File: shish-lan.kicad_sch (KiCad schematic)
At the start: 0 parts

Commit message: CuPhy: adding ports
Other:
- removed sheet buck_1V1
- removed sheet buck_2V5
- removed sheet buck_3V3
- removed sheet switch_decoupling
- removed sheet switch_gpios
- removed sheet switch_power
- added sheet switch_lan96455F (switch.kicad_sch)

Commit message: updating the projects
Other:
- sheet switch_lan96455F ports: added 1V1_EN, 25M_CLK_SWITCH, 2V5_EN, 3V3_EN, GGND, MIIM{MDIO,MDC}, PTP[0..3], RGMII{TXD[0..3], TX_CLK, TX_CTLR, RXD[0..3], RX_CLK, RX_CTLR}, SPI_SLV{DI,DO,nCS,CLK}, nRST_SWITCH; removed RGMII{TXD[0..3], TX_CLK, TX_CTLR, RXD[0..3], RX_CLK, RX_CTLR, MDIO, MDC},REF_CLK
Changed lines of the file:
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@@
 	)
 	(sheet
-		(at 191.77 45.72)
-		(size 91.44 41.91)
+		(at 182.88 44.45)
+		(size 91.44 92.71)
 		(exclude_from_sim no)
 		(in_bom yes)
@@
 		)
 		(property "Sheetname" "switch_lan96455F"
-			(at 191.77 45.0084 0)
+			(at 182.88 43.7384 0)
 			(effects
 				(font
@@
 		)
 		(property "Sheetfile" "switch.kicad_sch"
-			(at 191.77 88.2146 0)
+			(at 182.88 137.7446 0)
 			(effects
 				(font
@@
 		)
 		(pin "5-12V_INPUT" input
-			(at 191.77 50.8 180)
+			(at 182.88 113.03 180)
 			(effects
 				(font
@@
 			)
 		)
-		(pin "RGMII{TXD[0..3], TX_CLK, TX_CTLR, RXD[0..3], RX_CLK, RX_CTLR, MDIO, MDC},REF_CLK"
-			bidirectional
-			(at 191.77 55.88 180
-			)
+		(pin "RGMII{TXD[0..3], TX_CLK, TX_CTLR, RXD[0..3], RX_CLK, RX_CTLR}" bidirectional
+			(at 182.88 63.5 180)
 			(effects
 				(font
+					(size 1.27 1.27)
+				)
+				(justify left)
+			)
+		)
+		(pin "MIIM{MDIO,MDC}" bidirectional
+			(at 182.88 68.58 180)
+			(effects
+				(font
+					(size 1.27 1.27)
+				)
+				(justify left)
+			)
+		)
+		(pin "GGND" input
+			(at 182.88 115.57 180)
+			(effects
+				(font
+					(size 1.27 1.27)
+				)
+				(justify left)
+			)
+		)
+		(pin "nRST_SWITCH" input
+			(at 182.88 92.71 180)
+			(effects
+				(font
+					(size 1.27 1.27)
+				)
+				(justify left)
+			)
+		)
+		(pin "PTP[0..3]" input
+			(at 182.88 85.09 180)
+			(effects
+				(font
+					(size 1.27 1.27)
+				)
+				(justify left)
+			)
+		)
+		(pin "SPI_SLV{DI,DO,nCS,CLK}" bidirectional
+			(at 182.88 73.66 180)
+			(effects
+				(font
+					(size 1.27 1.27)
+				)
+				(justify left)
+			)
+		)
+		(pin "25M_CLK_SWITCH" input
+			(at 182.88 55.88 180)
+			(effects
+				(font
+					(size 1.27 1.27)
+				)
+				(justify left)
+			)
+		)
+		(pin "2V5_EN" input
+			(at 182.88 101.6 180)
+			(effects
+				(font
+					(size 1.27 1.27)
+				)
+				(justify left)
+			)
+		)
+		(pin "1V1_EN" input
+			(at 182.88 105.41 180)
+			(effects
+				(font
+					(size 1.27 1.27)
+				)
+				(justify left)
+			)
+		)
+		(pin "3V3_EN" input
+			(at 182.88 97.79 180)
+			(effects
+				(font

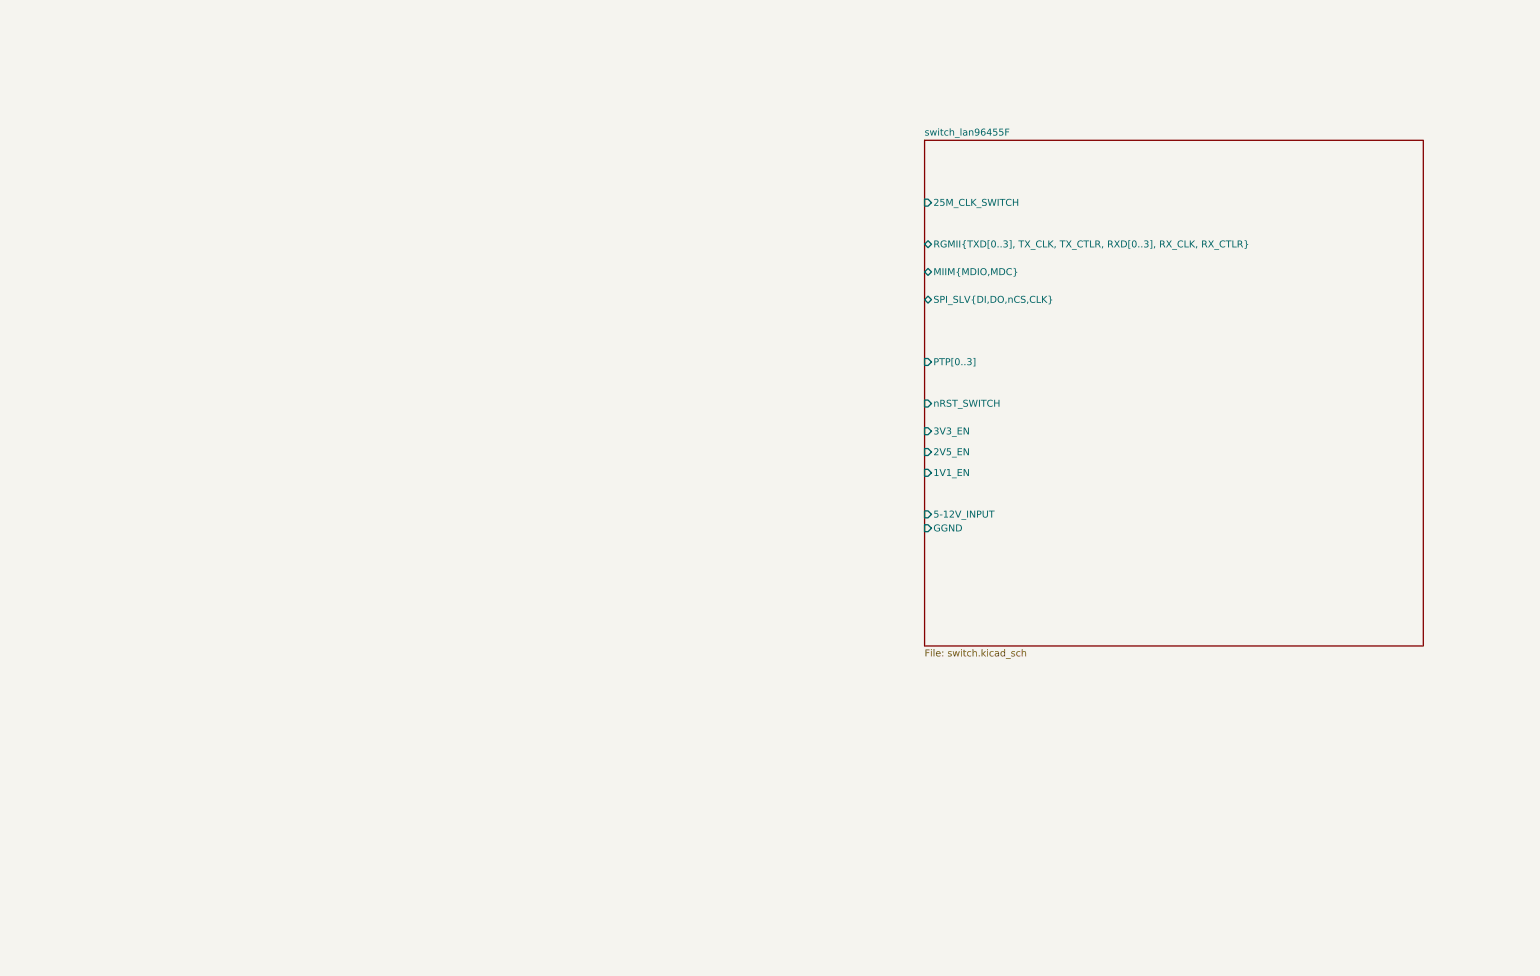
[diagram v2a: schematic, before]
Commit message: switch: finished 1st version
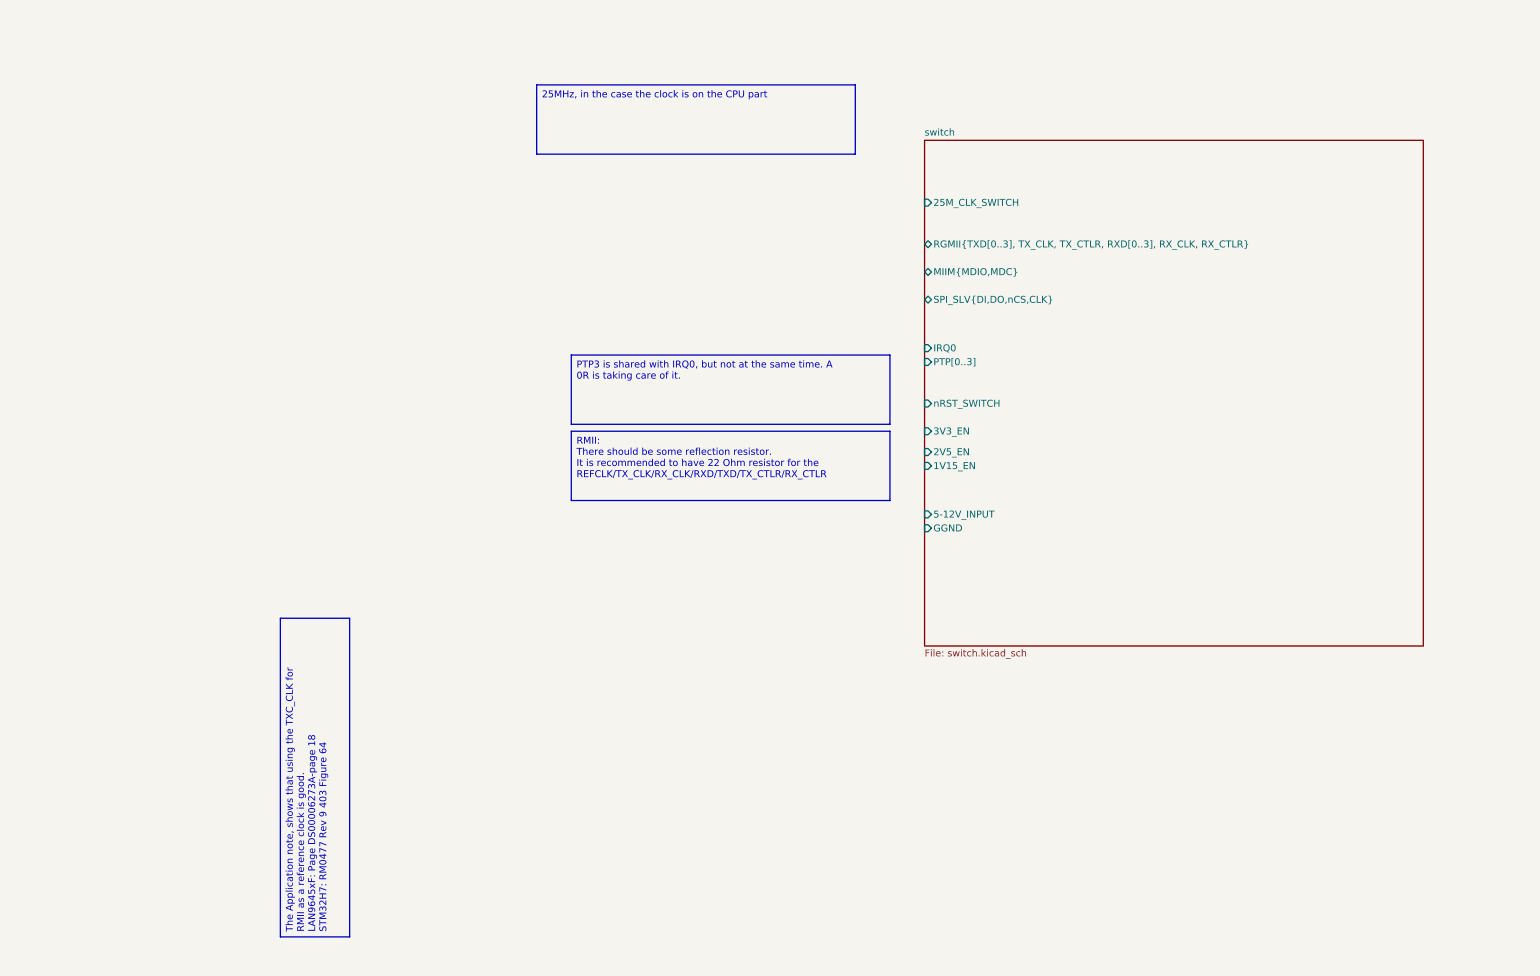
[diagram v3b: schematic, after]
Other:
- sheet switch_lan96455F renamed switch
- sheet switch ports: added 1V15_EN, IRQ0; removed 1V1_EN

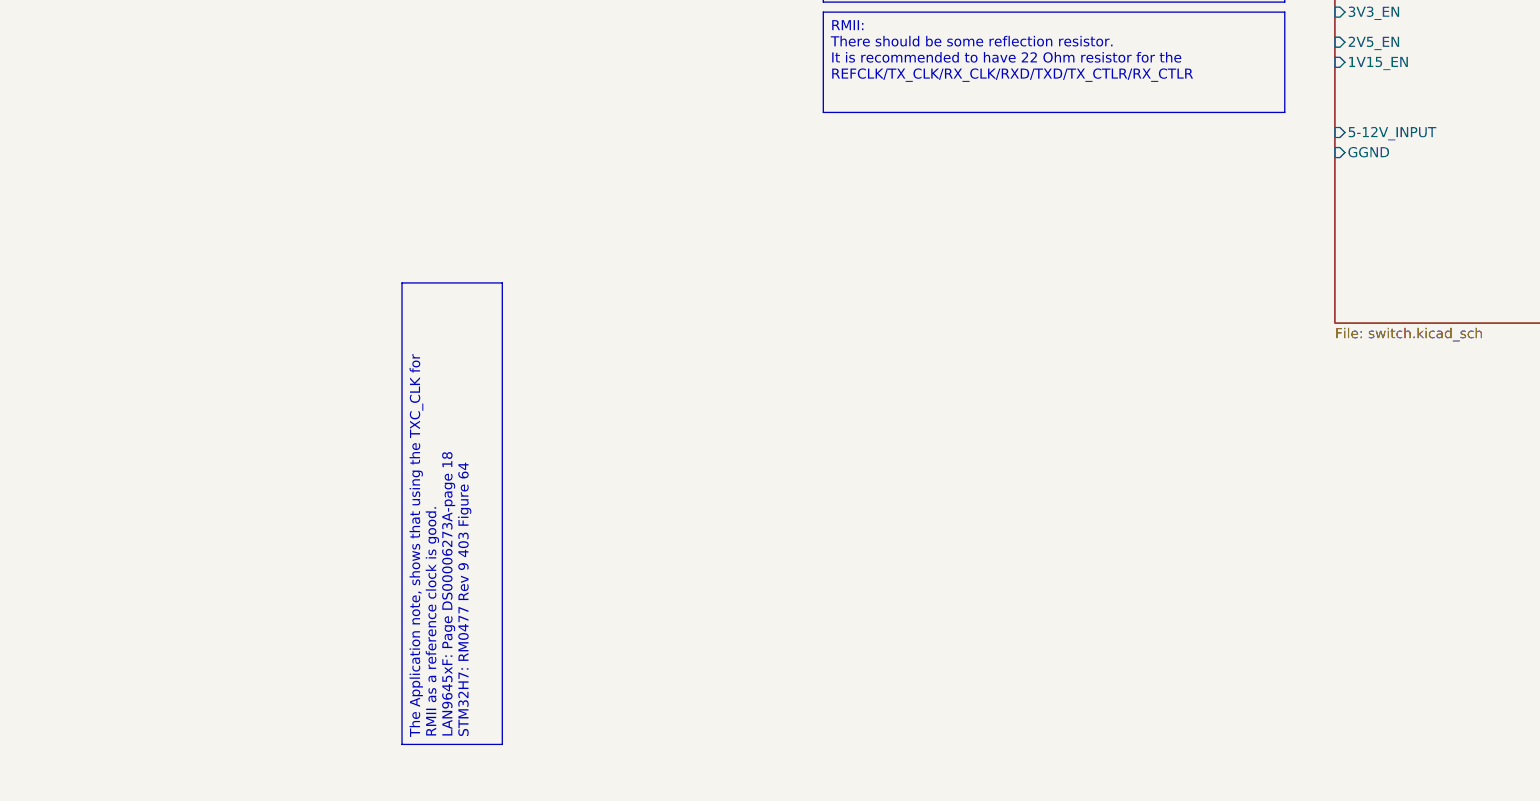
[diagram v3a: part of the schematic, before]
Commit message: adds GND test points because there is always one missing for the perfect measurement
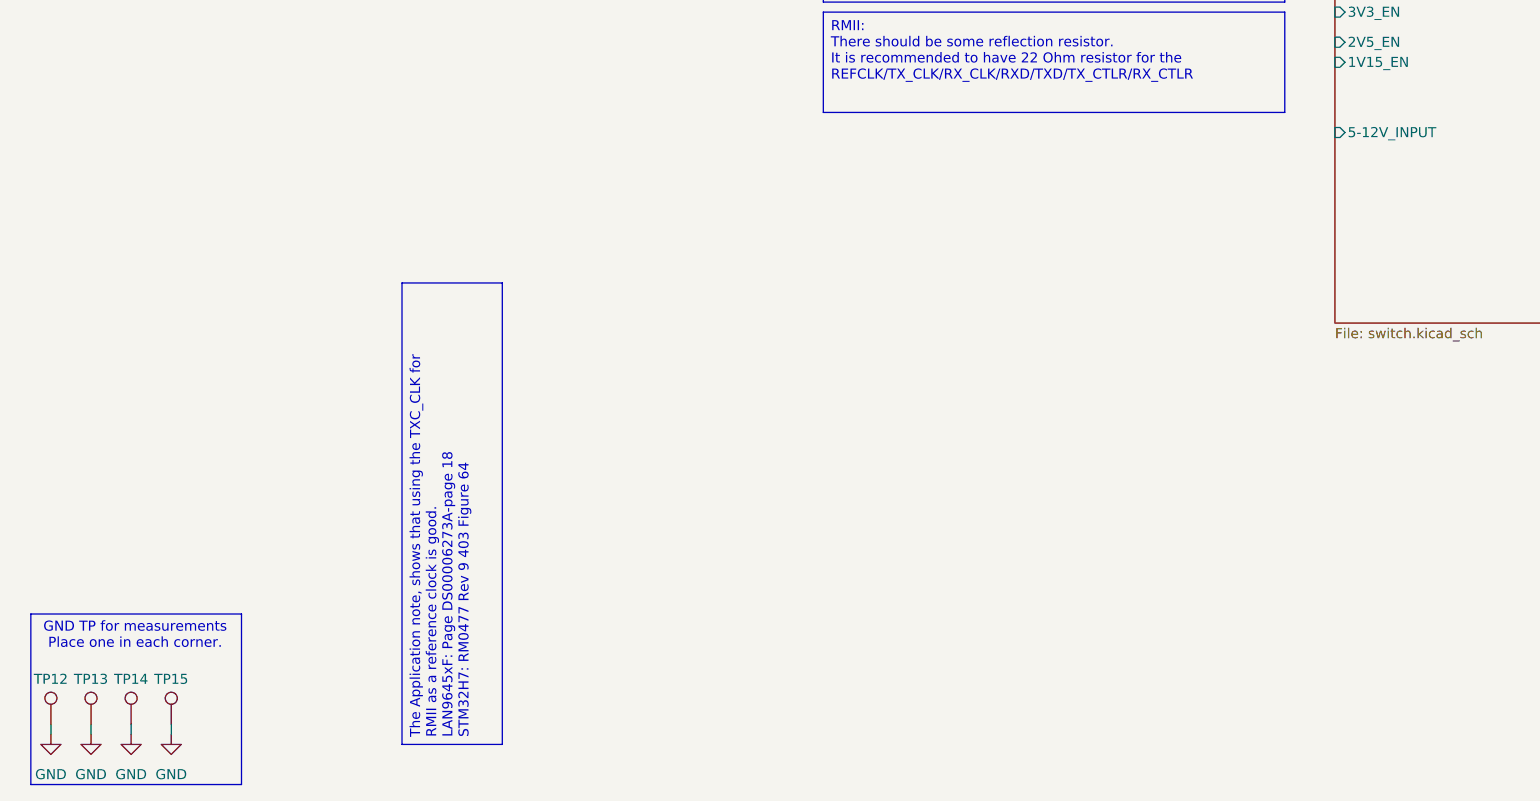
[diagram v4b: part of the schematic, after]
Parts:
- added TP12, TP13, TP14, TP15: ~, Connector_PinHeader_2.54mm:PinHeader_1x01_P2.54mm_Vertical, symbol KL_TP:TestPoint
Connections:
- new net GND: TP12.1, TP13.1, TP14.1, TP15.1
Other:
- sheet switch ports: added none; removed GGND
- note added: "GND TP for measurements Place one in each corner."

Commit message: updates project file and schematic. Refs: #1
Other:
- added sheet controller (controller.kicad_sch)
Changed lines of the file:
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@@
 	)
 	(sheet
-		(at 182.88 44.45)
-		(size 91.44 92.71)
+		(at 29.845 23.495)
+		(size 51.435 27.94)
 		(exclude_from_sim no)
 		(in_bom yes)
+		(on_board yes)
+		(dnp no)
+		(fields_autoplaced yes)
+		(stroke
+			(width 0.1524)
+			(type solid)
+		)
+		(fill
+			(color 0 0 0 0.0000)
+		)
+		(property "Sheetname" "controller"
+			(at 29.845 22.7834 0)
+			(effects
+				(font
+					(size 1.27 1.27)
+				)
+				(justify left bottom)
+			)
+		)
+		(property "Sheetfile" "controller.kicad_sch"
+			(at 29.845 52.0196 0)
+			(effects
+				(font
+					(size 1.27 1.27)
+				)
+				(justify left top)
+			)
+		)
+		(instances
+			(project "shish-lan"
+				(path "/d4536448-b109-4159-96e2-3dc21baf2d6e"
+					(page "8")
+				)
+			)
+		)
+	)
+	(sheet
+		(at 208.28 55.88)
+		(size 26.67 8.89)
+		(exclude_from_sim no)
+		(in_bom yes)
